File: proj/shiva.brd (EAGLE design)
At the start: 43.2 x 55.1 mm, 22 parts, among them J1 DM3D-SFDM, J2 ADAFRUIT_OLED_13, SW1 TACTSW_2CK_KXT3, SW2 TACTSW_2CK_KXT3, SW3 TACTSW_2CK_KXT3, SW4 TACTSW_2CK_KXT3, SW5 TACTSW_2CK_KXT3, SW6 TACTSW_2CK_KXT3, SW7 TACTSW_2CK_KXT3, U1 MCP23008QFN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

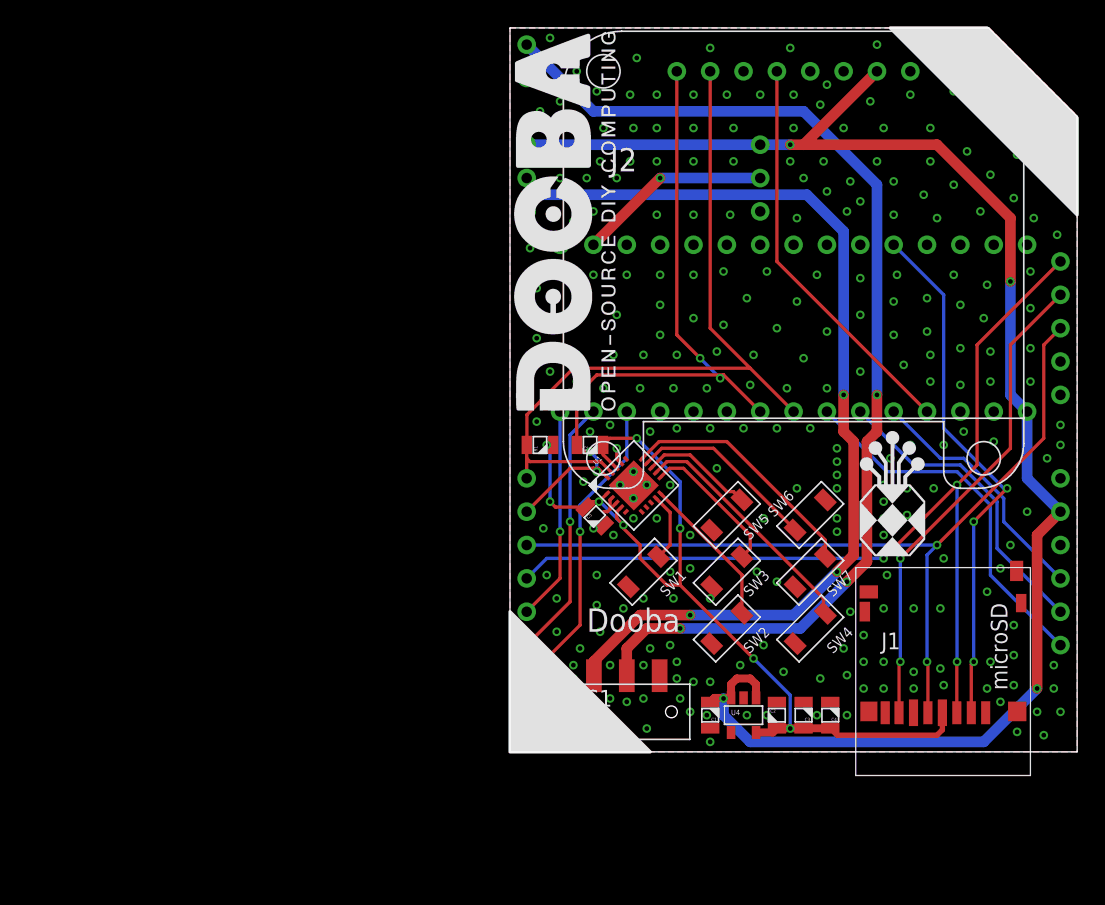
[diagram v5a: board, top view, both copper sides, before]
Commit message: Updated Shiva board to use smaller oled (128x32) and joystick instead of directional buttons Added Fiddle UI Board
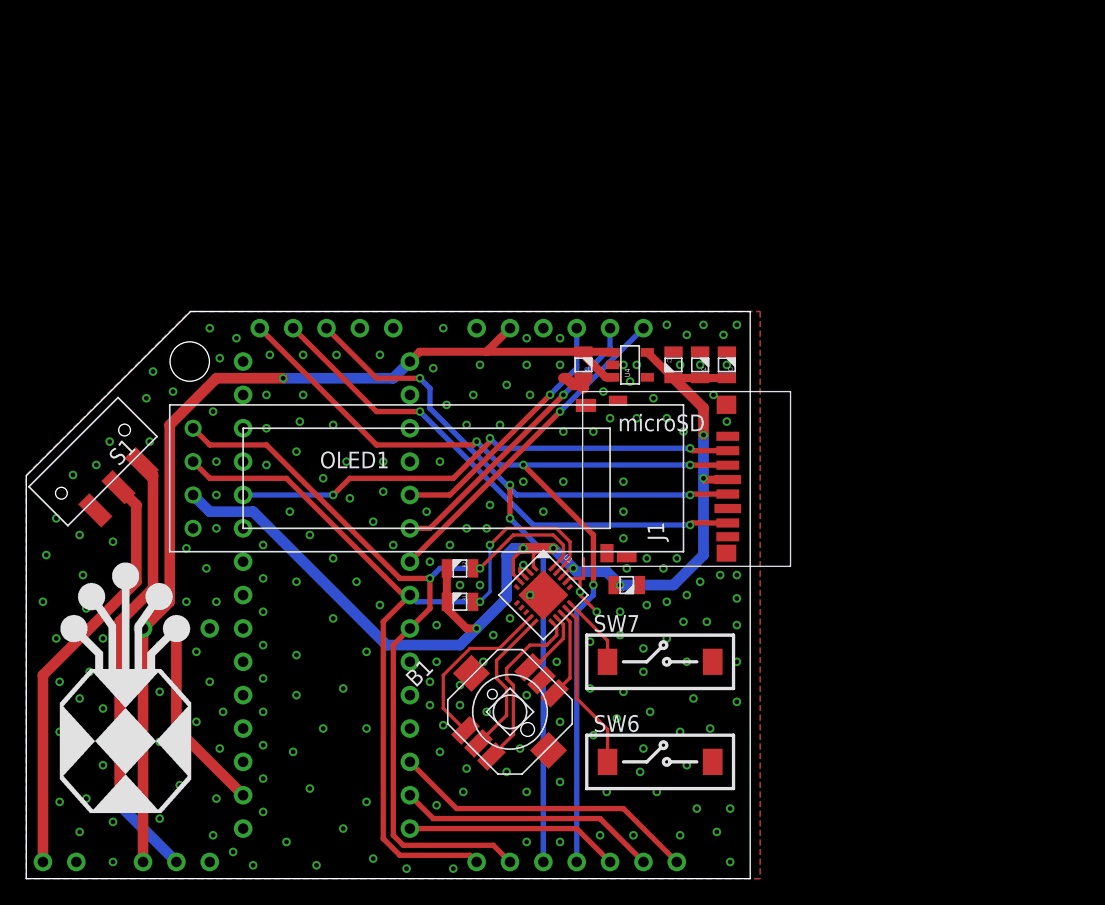
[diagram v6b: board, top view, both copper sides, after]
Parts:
- removed J2: ADAFRUIT_OLED_13, dooba:ADAFRUIT_OLED_13
- removed SW1, SW2, SW3, SW4, SW5: TACTSW_2CK_KXT3, dooba:CK_KXT3
- added B1: TACTSW_5WAYSMD-7X7, dooba:TACTSW-5WAY-7X7
- added OLED1: I2C-OLED-0.91, dooba:I2C-OLED-0.91
- SW6, SW7: value TACTSW_2CK_KXT3 -> TACTSW_2MICRO3X6; device dooba:CK_KXT3 -> dooba:TACTSW_MICRO3X6
- moved U3 61.3 mm to (27.9, 26.7), turned to 270 degrees
- moved S1 44.9 mm to (25.4, 48.3), turned to 225 degrees
- moved N1 40.5 mm to (43.2, 36.8), turned to 270 degrees
- moved C4 28.5 mm to (71.6, 55.6)
- moved C1 28.4 mm to (62.7, 55.6)
- moved U4 28.0 mm to (66.3, 55.6), turned to 90 degrees
- moved C2 27.8 mm to (69.6, 55.6)
- moved C3 27.3 mm to (73.7, 55.6)
- moved J1 24.3 mm to (72.4, 47.0), turned to 90 degrees
- moved SW6 22.0 mm to (68.6, 25.4), turned to 0 degrees
- moved U2 18.0 mm to (61.0, 38.1), turned to 270 degrees
- moved R2 13.7 mm to (53.3, 40.1), turned to 180 degrees
- moved R1 13.4 mm to (53.3, 37.6), turned to 180 degrees
- moved SW7 13.3 mm to (68.6, 33.0), turned to 0 degrees
- moved U1 10.8 mm to (59.7, 38.1), turned to 315 degrees
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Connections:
- net 3.3V: now also OLED1.VCC
- net 5.5V: no longer J2.VIN
- net GND: now also B1.5, B1.GND1, B1.GND2, OLED1.GND, SW6.2, SW7.2; no longer J2.GND, SW1.P$2, SW2.P$2, SW3.P$2, SW4.P$2, SW5.P$2, SW6.P$2, SW7.P$2
- net I2C_SCL: now also OLED1.SCL; no longer J2.CLK
- net I2C_SDA: now also OLED1.SDA; no longer J2.DATA
- net N$1: now also B1.1; no longer SW1.P$1
- net N$2: now also B1.2; no longer SW2.P$1
- net N$3: now also B1.3; no longer SW3.P$1
- net N$4: now also B1.6, U1.13; no longer SW4.P$1, U1.12
- net N$5: now also B1.4, U1.12; no longer SW5.P$1, U1.13
- net N$6: now also SW6.1; no longer SW6.P$1
- net N$7: now also SW7.1; no longer SW7.P$1
- net OLED_RST: no longer J2.RST
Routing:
- net VBAT: track 83.2 -> 32.0 mm, vias 3 -> 0
- net 5.5V: track 119.0 -> 75.9 mm, vias 4 -> 1
- net N$11: track 75.0 -> 33.5 mm, vias 3 -> 1
- net OLED_RST: track 30.6 -> 0.00 mm
- net 3.3V: track 70.3 -> 86.6 mm, vias 8 -> 7
- net N$7: track 18.9 -> 5.67 mm
- net I2C_SDA: track 55.8 -> 67.8 mm, vias 4 -> 2
- net N$4: track 18.6 -> 6.96 mm
- net I2C_SCL: track 58.8 -> 68.5 mm, vias 0 -> 2
- net N$1: track 5.29 -> 13.4 mm
- net GND: track 4.20 -> 11.9 mm, vias 262 -> 223
- net N$5: track 8.76 -> 5.43 mm
- net AMP_VUPDN: track 28.3 -> 25.1 mm, vias 0 -> 1
- net N$3: track 11.1 -> 13.7 mm
- net SPI_MISO: track 36.9 -> 39.4 mm
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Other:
- board size 43.2 x 55.1 mm -> 55.1 x 43.2 mm
- board text removed: "Dooba"
